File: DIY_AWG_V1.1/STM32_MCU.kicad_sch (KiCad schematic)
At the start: 28 parts, among them J1 Conn_01x04_Pin, SW1 SW_Push, SW2 SW_Push, U10 STM32G473VETx, U8 USBLC6-2SC6, U9 161N-4BVS11, X1 SX2M8.000B10F20TNN

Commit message: Updated schematics
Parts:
- removed TP10: TestPoint, symbol Connector:TestPoint
- added J3: Conn_01x02_Pin, Connector_PinHeader_2.54mm:PinHeader_1x02_P2.54mm_Vertical, symbol Connector:Conn_01x02_Pin
- C42: footprint (none) -> Capacitor_SMD:C_0402_1005Metric
- J2: renamed from J1; footprint (none) -> Connector_PinHeader_2.54mm:PinHeader_1x04_P2.54mm_Vertical
- TP11: footprint (none) -> TestPoint:TestPoint_Pad_D2.0mm
- TP12: renamed from TP9; footprint (none) -> TestPoint:TestPoint_Pad_D2.0mm
- renumbered C37 to C31, C86 to C34, C87 to C37
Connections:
- net GND: now also TP11.1
- net UART4_RX: now also J3.2 (Pin_2); no longer TP11.1
- net UART4_TX: now also J3.1 (Pin_1)
- net +5V renamed +VSW5V0

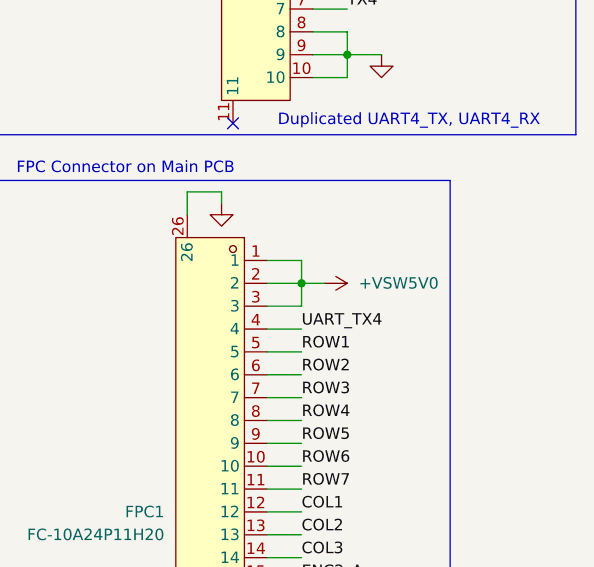
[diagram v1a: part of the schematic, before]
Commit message: Updated PCB design, uploaded necessary footprints and symbols for some components
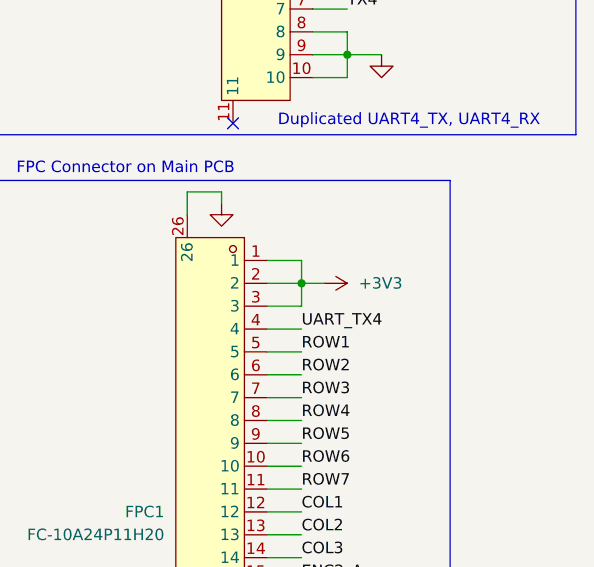
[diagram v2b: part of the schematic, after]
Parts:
- TP11, TP12: footprint TestPoint:TestPoint_Pad_D2.0mm -> TestPoint:TestPoint_Pad_D1.0mm
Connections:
- net +3V3: now also FPC1.1, FPC1.2, FPC1.3
- net +VSW5V0: no longer FPC1.1, FPC1.2, FPC1.3
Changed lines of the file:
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@@
 			)
 		)
-		(property "Footprint" "TestPoint:TestPoint_Pad_D2.0mm"
+		(property "Footprint" "TestPoint:TestPoint_Pad_D1.0mm"
 			(at 43.18 154.94 0)
 			(hide yes)
@@
 	)
 	(symbol
-		(lib_id "power:+VSW")
-		(at 255.27 69.85 270)
-		(unit 1)
-		(body_style 1)
-		(exclude_from_sim no)
-		(in_bom yes)
-		(on_board yes)
-		(in_pos_files yes)
-		(dnp no)
-		(fields_autoplaced yes)
-		(property "Reference" "#PWR0101"
-			(at 251.46 69.85 0)
-			(hide yes)
-			(show_name no)
-			(do_not_autoplace no)
-			(effects
-				(font
-					(size 1.27 1.27)
-				)
-			)
-		)
-		(property "Value" "+VSW5V0"
-			(at 259.08 69.8499 90)
-			(show_name no)
-			(do_not_autoplace no)
-			(effects
-				(font
-					(size 1.27 1.27)
-				)
-				(justify left)
-			)
-		)
-		(property "Footprint" ""
-			(at 255.27 69.85 0)
-			(hide yes)
-			(show_name no)
-			(do_not_autoplace no)
-			(effects
-				(font
-					(size 1.27 1.27)
-				)
-			)
-		)
-		(property "Datasheet" ""
-			(at 255.27 69.85 0)
-			(hide yes)
-			(show_name no)
-			(do_not_autoplace no)
-			(effects
-				(font
-					(size 1.27 1.27)
-				)
-			)
-		)
-		(property "Description" "Power symbol creates a global label with name \"+VSW\""
-			(at 255.27 69.85 0)
-			(hide yes)
-			(show_name no)
-			(do_not_autoplace no)
-			(effects
-				(font
-					(size 1.27 1.27)
-				)
-			)
-		)
-		(pin "1"
-		)
-		(instances
-			(project "DIY_AWG_V1.1"
-				(path "/508078af-d961-4af3-840e-a064a9f8d5bc/aaba8d51-2713-41de-9761-99ebb3cee83e"
-					(reference "#PWR0101")
-					(unit 1)
-				)
-			)
-		)
-	)
-	(symbol
 		(lib_id "Device:C")
 		(at 166.37 31.75 0)
@@
 			)
 		)
-		(property "Footprint" "TestPoint:TestPoint_Pad_D2.0mm"
+		(property "Footprint" "TestPoint:TestPoint_Pad_D1.0mm"
 			(at 29.21 148.59 0)
 			(hide yes)
@@
 					(unit 1)
 				)
+			)
+		)
+	)
+	(symbol
+		(lib_id "power:+3V3")
+		(at 255.27 69.85 270)
+		(unit 1)
+		(body_style 1)
+		(exclude_from_sim no)
+		(in_bom yes)
+		(on_board yes)
+		(in_pos_files yes)
+		(dnp no)
+		(fields_autoplaced yes)
+		(property "Reference" "#PWR0101"
+			(at 251.46 69.85 0)
+			(hide yes)
+			(show_name no)
+			(do_not_autoplace no)
+			(effects
+				(font
+					(size 1.27 1.27)
+				)
+			)
+		)
+		(property "Value" "+3V3"
+			(at 259.08 69.8499 90)
+			(show_name no)
+			(do_not_autoplace no)
+			(effects
+				(font
+					(size 1.27 1.27)
+				)
+				(justify left)
+			)
+		)
+		(property "Footprint" ""
+			(at 255.27 69.85 0)
+			(hide yes)
+			(show_name no)
+			(do_not_autoplace no)
+			(effects
+				(font
+					(size 1.27 1.27)
+				)
+			)
+		)
+		(property "Datasheet" ""
+			(at 255.27 69.85 0)
+			(hide yes)
+			(show_name no)
+			(do_not_autoplace no)
+			(effects
+				(font
+					(size 1.27 1.27)
+				)
+			)
+		)
+		(property "Description" "Power symbol creates a global label with name \"+3V3\""
+			(at 255.27 69.85 0)
+			(hide yes)
+			(show_name no)
+			(do_not_autoplace no)
+			(effects
+				(font
+					(size 1.27 1.27)
+				)
+			)
+		)
+		(pin "1"
+		)
+		(instances
+			(project "DIY_AWG_V1.1"
+				(path "/508078af-d961-4af3-840e-a064a9f8d5bc/aaba8d51-2713-41de-9761-99ebb3cee83e"
+					(reference "#PWR0101")
+					(unit 1)
+				)

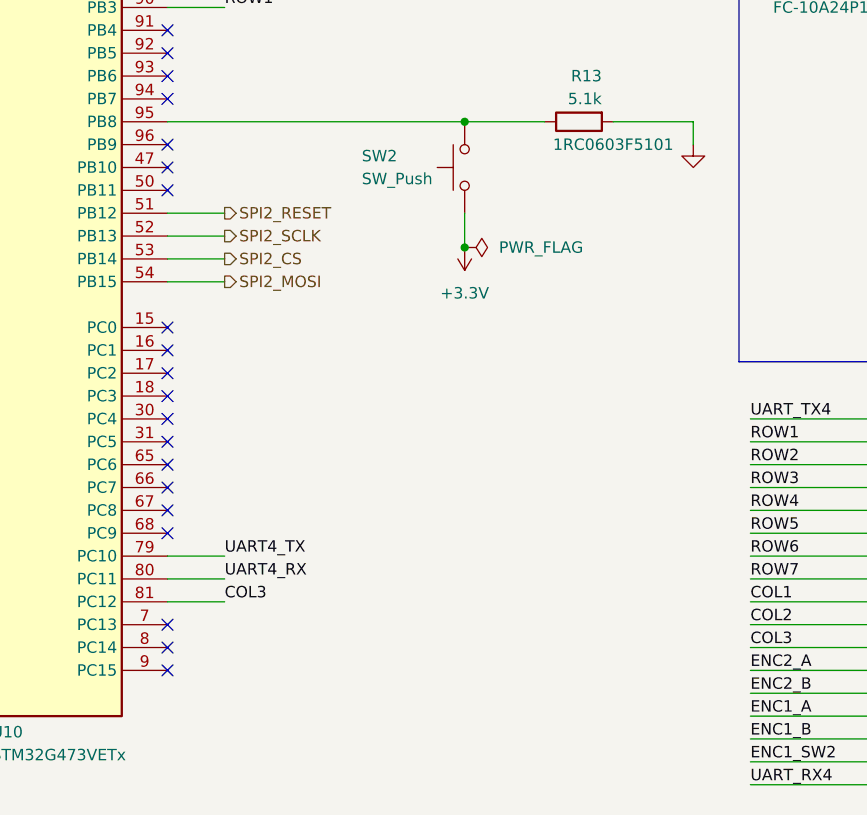
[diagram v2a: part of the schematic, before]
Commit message: Edited the electrical schematics, PCB design
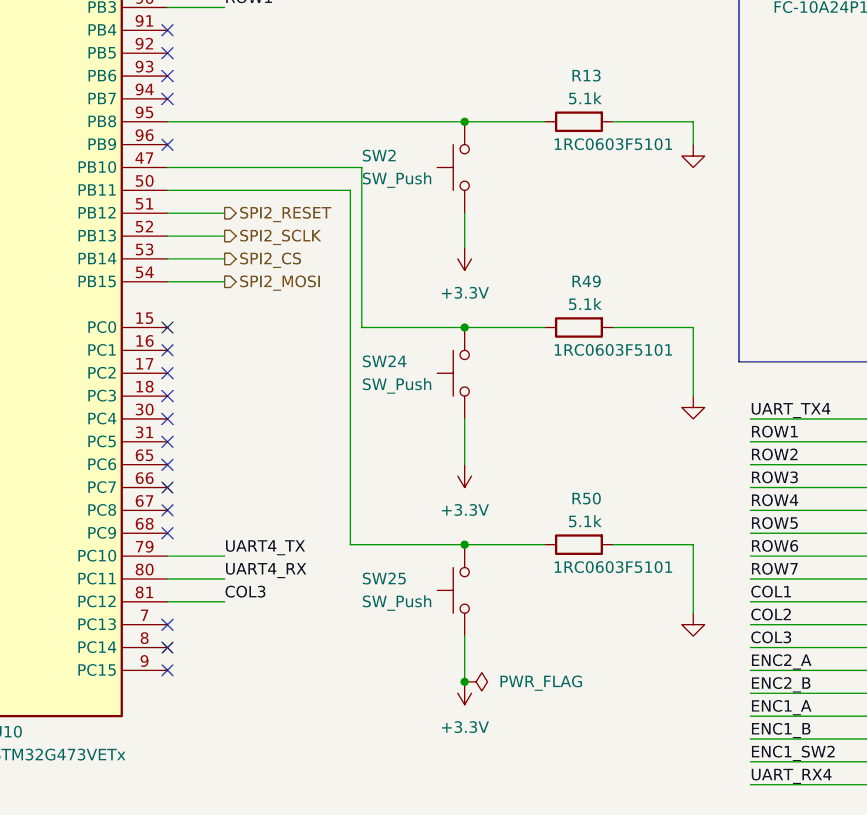
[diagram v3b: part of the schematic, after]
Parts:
- added R49, R50: 5.1k, Resistor_SMD:R_0603_1608Metric, symbol Device:R
- added SW24, SW25: SW_Push, easyeda2kicad:SW-SMD_L6.1-W3.5-LS8.6, symbol Switch:SW_Push
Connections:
- net +3.3V: now also SW24.1, SW25.1
- net GND: now also R49.2, R50.2
- net at U10.47 (PB10): now also R49.1, SW24.2
- net at U10.50 (PB11): now also R50.1, SW25.2
- no-connect marks 52 -> 50

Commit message: Updated schematic PCB design
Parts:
- renumbered R11 to R18, R12 to R19, R13 to R20, R49 to R21, R50 to R22, SW24 to SW3, SW25 to SW4, TP11 to TP17, TP12 to TP18

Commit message: Updated PCB schematics
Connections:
- net UART4_RX: no longer FPC2.6, J3.2 (Pin_2)
- net UART4_TX: no longer FPC2.5, J3.1 (Pin_1)
- net UART_RX4: now also FPC2.6, J3.2 (Pin_2)
- net UART_TX4: now also FPC2.5, J3.1 (Pin_1)
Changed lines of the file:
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@@
 		)
 	)
-	(label "UART4_TX"
+	(label "UART_TX4"
 		(at 257.81 34.29 0)
 		(effects
@@
 		)
 	)
-	(label "UART4_RX"
+	(label "UART_RX4"
 		(at 257.81 36.83 0)
 		(effects

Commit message: Updated PCB schematic
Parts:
- added LED11: XL-1608UBC-04, easyeda2kicad:LED0603-RD_BLUE, symbol easyeda2kicad:XL-1608UBC-04
- added R54: 1k, Resistor_SMD:R_0603_1608Metric, symbol Device:R
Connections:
- net +3.3V: now also R54.2
- net at U10.7 (PC13): now also LED11.1 (K)
- new net: LED11.2 (A), R54.1
- no-connect marks 50 -> 49
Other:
- note added: "To indicate code is running"

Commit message: Updated PCB schematic
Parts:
- added LED12: BL-HJC36G-AV-TRB, easyeda2kicad:LED0603-R-RD_AMBER, symbol easyeda2kicad:BL-HJC36G-AV-TRB
- added LED13: XL-1608SURC-06, easyeda2kicad:LED0603-RD_RED, symbol easyeda2kicad:XL-1608SURC-06
- added R55, R56: 1k, Resistor_SMD:R_0603_1608Metric, symbol Device:R
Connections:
- net +3.3V is gone; now on net +3V3: R54.2, SW2.1, SW3.1, SW4.1
- net +3V3: now also R55.2, R56.2
- net COL1: now also FPC1.15; no longer FPC1.12
- net COL2: now also FPC1.16; no longer FPC1.13
- net COL3: now also FPC1.17; no longer FPC1.14
- net ENC1_A: now also FPC1.21; no longer FPC1.17
- net ENC1_B: now also FPC1.22; no longer FPC1.18
- net ENC1_SW2: now also FPC1.23; no longer FPC1.19
- net ENC2_A: now also FPC1.19; no longer FPC1.15
- net ENC2_B: now also FPC1.20; no longer FPC1.16
- net FSELECT: now also U10.58 (PD11); no longer U10.56 (PD9)
- net GND: now also FPC1.18, FPC1.4, FPC1.7; no longer FPC1.21, FPC1.22, FPC1.23
- net ROW1: now also FPC1.8; no longer FPC1.5
- net ROW2: now also FPC1.9; no longer FPC1.6
- net ROW3: now also FPC1.10; no longer FPC1.7
- net ROW4: now also FPC1.11; no longer FPC1.8
- net ROW5: now also FPC1.12; no longer FPC1.9
- net ROW6: now also FPC1.13; no longer FPC1.10
- net ROW7: now also FPC1.14; no longer FPC1.11
- net RX4: now also U10.56 (PD9); no longer U10.70 (PA9)
- net TX4: now also U10.55 (PD8); no longer U10.69 (PA8)
- net UART_RX4: now also FPC1.6, U10.71 (PA10); no longer FPC1.20
- net UART_TX4: now also FPC1.5, U10.70 (PA9); no longer FPC1.4
- net at U10.32 (PB0): now also LED12.2 (C)
- net at U10.33 (PB1): now also LED13.1 (K)
- new net: LED13.2 (A), R56.1
- new net: LED12.1 (A), R55.1
- no-connect marks 49 -> 45
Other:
- note added: "4.7nF MLCC (2): 04023C472KAT2A (2) 100nF MLCC (8): C0603C104J3RACTU (8) 3.3uF MLCC (1): CL21B335KAFNFNE (1) 10uF MLCC (1): CL10A106KP8NNNC (1) 22uF MLCC (1): GRM31CR61C226KE15L (1) 1k Resistor (3): THD03G1001BT (3) 5.1k Resistor (3): 1RC0603F5101 (3)"
- note added: "BOOT0"
- note added: "ERR_ON"
- note added: "OUT_ON"
- note added: "To indicate code is running INIT_RUN"
- note added: "User-Def 1"
- note added: "User-Def 2"
- note removed: "4.7nF MLCC (2): 04023C472KAT2A (2) 100nF MLCC (8): C0603C104J3RACTU (8) 3.3uF MLCC (1): CL21B335KAFNFNE (1) 10uF MLCC (1): CL10A106KP8NNNC (1) 22uF MLCC (1): GRM31CR61C226KE15L (1) 5.1k Resistor (3): 1RC0603F5101 (3)"
- note removed: "Remove ATT1 pins"
- note removed: "To indicate code is running"

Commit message: Updated PCB schematic
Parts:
- added C86: 100n, Capacitor_SMD:C_0603_1608Metric, symbol Device:C
- added TP28, TP29: TestPoint, TestPoint:TestPoint_Pad_D1.0mm, symbol Connector:TestPoint
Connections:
- net COL1: now also FPC1.10; no longer FPC1.15
- net COL2: now also FPC1.9; no longer FPC1.16
- net COL3: now also FPC1.8; no longer FPC1.17
- net ENC2_A: now also FPC1.20, U10.34 (PB2); no longer FPC1.19, U10.1 (PE2)
- net ENC2_B: now also FPC1.19, U10.17 (PC2); no longer FPC1.20, U10.2 (PE3)
- net GND: now also C86.2
- net MUX1_A0: now also U10.30 (PC4); no longer U10.59 (PD12)
- net MUX1_A1: now also U10.31 (PC5); no longer U10.60 (PD13)
- net MUX1_EN: now also U10.29 (PA7); no longer U10.61 (PD14)
- net ROW1: now also FPC1.17; no longer FPC1.8
- net ROW2: now also FPC1.16; no longer FPC1.9
- net ROW3: now also FPC1.15; no longer FPC1.10
- net ROW4: now also FPC1.14; no longer FPC1.11
- net ROW5: now also FPC1.13; no longer FPC1.12
- net ROW6: now also FPC1.12; no longer FPC1.13
- net ROW7: now also FPC1.11; no longer FPC1.14
- net RX4: now also TP28.1; no longer U10.56 (PD9)
- net TX4: now also TP29.1; no longer U10.55 (PD8)
- net UART_RX4: now also FPC1.5; no longer FPC1.6
- net UART_TX4: now also FPC1.6; no longer FPC1.5
- net VBUS: now also C86.1
- net USER_DEF1: now reaches R21.1, SW3.2, U10.47 (PB10)
- net BOOT0: now reaches R20.1, SW2.2, U10.95 (PB8)
- net at U10.33 (PB1): no longer LED13.1 (K)
- net ERR_ON: now reaches U10.16 (PC1)
- net ERR_ON: now also LED13.1 (K)
- net OUT_ON: now reaches U10.18 (PC3)
- net OUT_ON: now also LED12.2 (C)
- net INIT_RUN: now reaches U10.19 (PF2)
- net INIT_RUN: now also LED11.1 (K)
- net at U10.32 (PB0): no longer LED12.2 (C)
- net USER_DEF2: now reaches R22.1, SW4.2, U10.50 (PB11)
- net at U10.7 (PC13): no longer LED11.1 (K)
- net UART4_RX: no longer names the net of U10.80 (PC11)
- net UART4_TX: no longer names the net of U10.79 (PC10)
- net USB_DM renamed USB_DN
- no-connect marks 45 -> 49
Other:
- note added: "4.7nF MLCC (2): 04023C472KAT2A (2) 100nF MLCC (9): C0603C104J3RACTU (9) 3.3uF MLCC (1): CL21B335KAFNFNE (1) 10uF MLCC (1): CL10A106KP8NNNC (1) 22uF MLCC (1): GRM31CR61C226KE15L (1) 1k Resistor (3): THD03G1001BT (3) 5.1k Resistor (3): 1RC0603F5101 (3)"
- note added: "Buttons and Indicators"
- note added: "Double Check RX4 TX4 Connection from DWIN Display"
- note removed: "4.7nF MLCC (2): 04023C472KAT2A (2) 100nF MLCC (8): C0603C104J3RACTU (8) 3.3uF MLCC (1): CL21B335KAFNFNE (1) 10uF MLCC (1): CL10A106KP8NNNC (1) 22uF MLCC (1): GRM31CR61C226KE15L (1) 1k Resistor (3): THD03G1001BT (3) 5.1k Resistor (3): 1RC0603F5101 (3)"
- note removed: "Duplicated UART4_TX, UART4_RX"
- moved on the sheet: C31, C32, C34, C37, FPC1, FPC2, J3, LED11, LED12, LED13, R18, R19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
